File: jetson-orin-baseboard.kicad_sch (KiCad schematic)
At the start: 4 parts

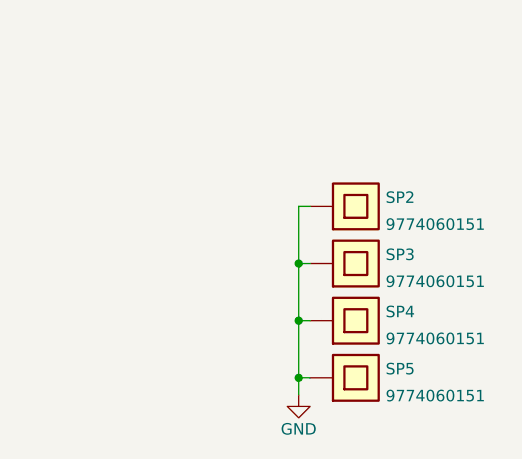
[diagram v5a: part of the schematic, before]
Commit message: Reannotate parts
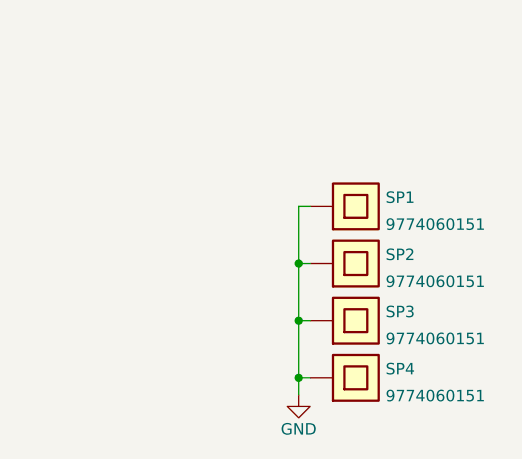
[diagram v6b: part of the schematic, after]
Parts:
- renumbered SP2 to SP1, SP3 to SP2, SP4 to SP3, SP5 to SP4
